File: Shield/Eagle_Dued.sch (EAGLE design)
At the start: 36 parts

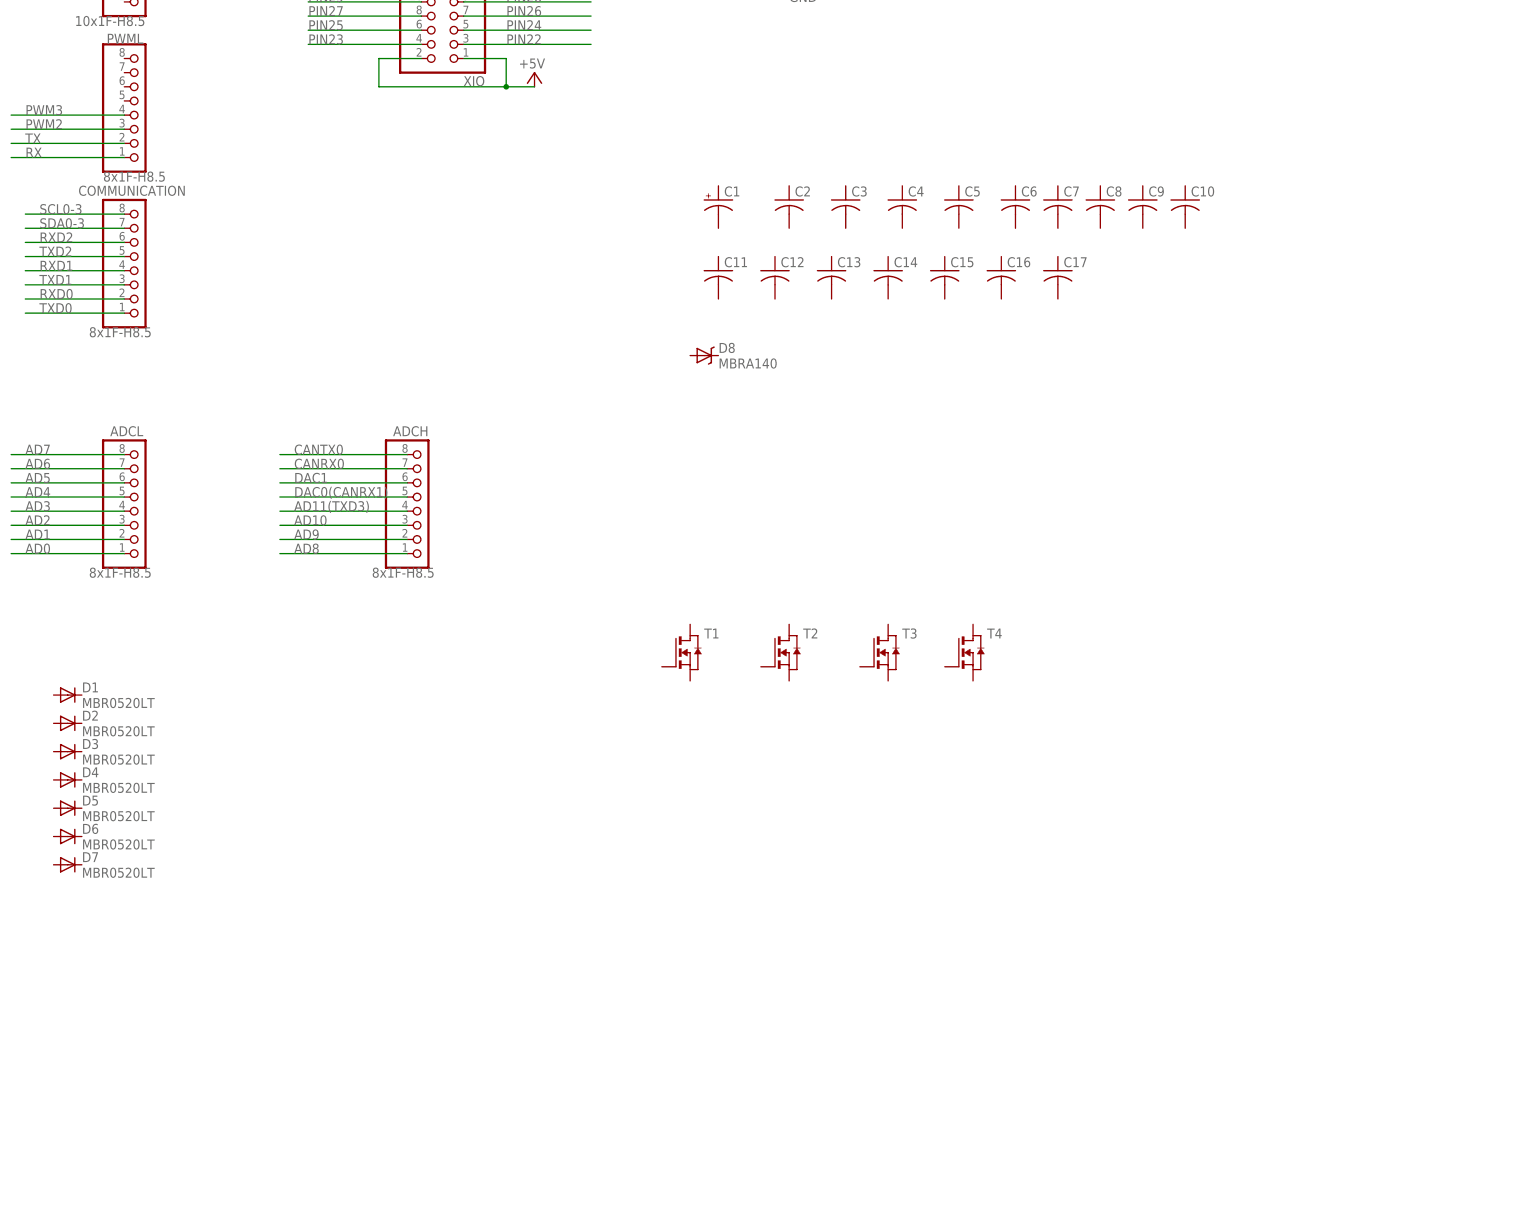
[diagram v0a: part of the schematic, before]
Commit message: More updates to schematic for Shield
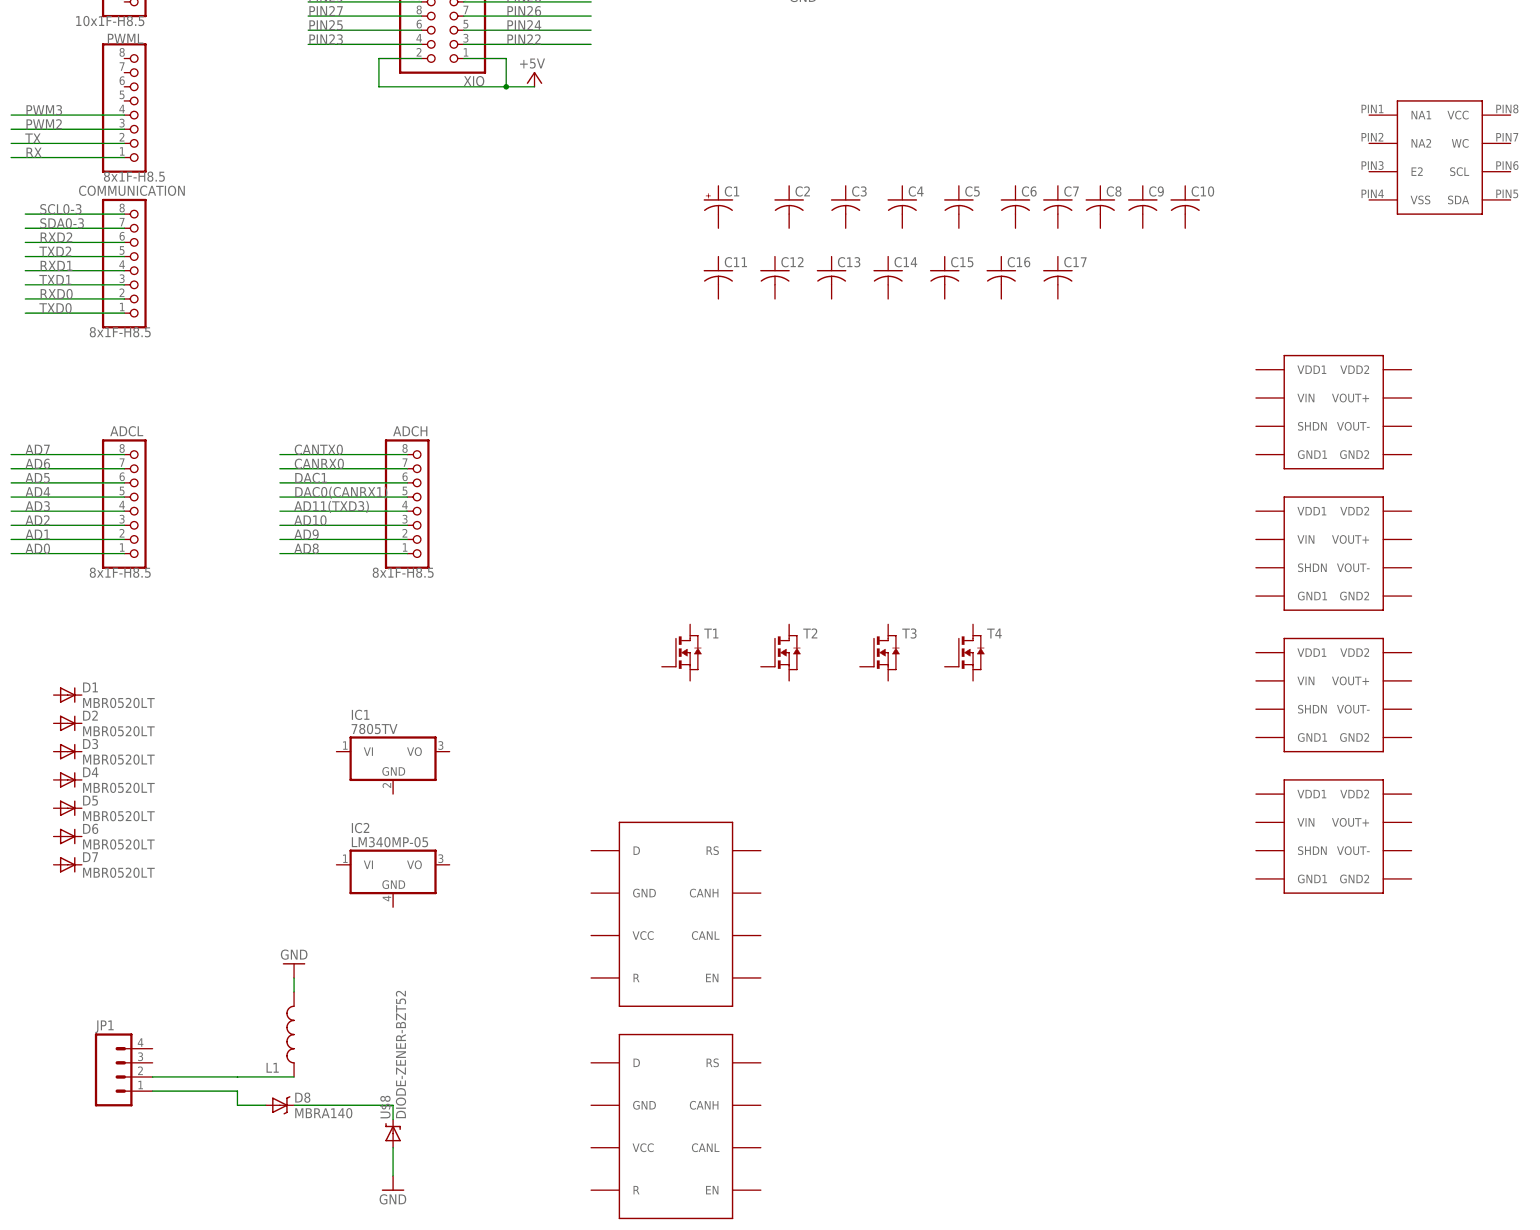
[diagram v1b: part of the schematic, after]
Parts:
- added IC1: 7805TV, linear:7805TV
- added IC2: LM340MP-05, linear:LM340MP-05
- added JP1: (no value), SparkFun-Connectors:M04PTH
- added L1: (no value), SparkFun-Passives:INDUCTOR1206H*
- added U$1, U$2, U$3, U$4: ACPL-C87A-000E, ck_custom:ACPL-C87A-000E
- added U$5: M24M02-DRMN6TP, ck_custom:M24M02-DRMN6TP
- added U$6, U$7: SN65HVD234, ck_custom:SN65HVD234
- added U$8: DIODE-ZENER-BZT52, SparkFun-DiscreteSemi:DIODE-ZENER-BZT52
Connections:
- new net N$1: JP1.2, L1.1
- new net N$2: D8.A, JP1.1
- new net N$3: D8.C, U$8.C
- net GND: now also L1.2, U$8.A
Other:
- moved on the sheet: D8
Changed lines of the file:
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@@
 <part name="C17" library="rcl" deviceset="C-US" device="C0603"/>
 <part name="D8" library="SparkFun-DiscreteSemi" deviceset="MBRA140" device=""/>
+<part name="U$1" library="ck_custom" deviceset="ACPL-C87A-000E" device=""/>
+<part name="U$2" library="ck_custom" deviceset="ACPL-C87A-000E" device=""/>
+<part name="U$3" library="ck_custom" deviceset="ACPL-C87A-000E" device=""/>
+<part name="U$4" library="ck_custom" deviceset="ACPL-C87A-000E" device=""/>
+<part name="U$5" library="ck_custom" deviceset="M24M02-DRMN6TP" device=""/>
+<part name="U$6" library="ck_custom" deviceset="SN65HVD234" device=""/>
+<part name="U$7" library="ck_custom" deviceset="SN65HVD234" device=""/>
+<part name="IC1" library="linear" deviceset="78*" device="TV" technology="05"/>
+<part name="IC2" library="linear" deviceset="LM340?-*" device="MP" technology="05"/>
+<part name="L1" library="SparkFun-Passives" deviceset="INDUCTOR" device="H*" technology="1206"/>
+<part name="JP1" library="SparkFun-Connectors" deviceset="M04" device="PTH"/>
+<part name="GND1" library="supply1" deviceset="GND" device=""/>
+<part name="U$8" library="SparkFun-DiscreteSemi" deviceset="DIODE-ZENER" device="-BZT52"/>
+<part name="GND2" library="supply1" deviceset="GND" device=""/>
 </parts>
 <sheets>
@@
 <instance part="C16" gate="G$1" x="464.82" y="119.38"/>
 <instance part="C17" gate="G$1" x="474.98" y="119.38"/>
-<instance part="D8" gate="G$1" x="411.48" y="104.14"/>
+<instance part="D8" gate="G$1" x="335.28" y="-30.48"/>
+<instance part="U$1" gate="G$1" x="515.62" y="83.82"/>
+<instance part="U$2" gate="G$1" x="515.62" y="58.42"/>
+<instance part="U$3" gate="G$1" x="515.62" y="33.02"/>
+<instance part="U$4" gate="G$1" x="515.62" y="7.62"/>
+<instance part="U$5" gate="G$1" x="535.94" y="129.54"/>
+<instance part="U$6" gate="G$1" x="396.24" y="-12.7"/>
+<instance part="U$7" gate="G$1" x="396.24" y="-50.8"/>
+<instance part="IC1" gate="A1" x="355.6" y="33.02"/>
+<instance part="IC2" gate="A" x="355.6" y="12.7"/>
+<instance part="L1" gate="G$1" x="337.82" y="-17.78" rot="R180"/>
+<instance part="JP1" gate="G$1" x="307.34" y="-25.4"/>
+<instance part="GND1" gate="1" x="337.82" y="-5.08" rot="R180"/>
+<instance part="U$8" gate="G$1" x="355.6" y="-35.56" rot="R90"/>
+<instance part="GND2" gate="1" x="355.6" y="-45.72"/>
 </instances>
 <busses>
@@
 <pinref part="GND6" gate="1" pin="GND"/>
 </segment>
+<segment>
+<pinref part="L1" gate="G$1" pin="2"/>
+<pinref part="GND1" gate="1" pin="GND"/>
+<wire x1="337.82" y1="-10.16" x2="337.82" y2="-7.62" width="0.1524" layer="91"/>
+</segment>
+<segment>
+<pinref part="U$8" gate="G$1" pin="A"/>
+<pinref part="GND2" gate="1" pin="GND"/>
+<wire x1="355.6" y1="-38.1" x2="355.6" y2="-43.18" width="0.1524" layer="91"/>
+</segment>
 </net>
 <net name="VIN" class="0">
@@
 </segment>
 </net>
+<net name="N$1" class="0">
+<segment>
+<pinref part="JP1" gate="G$1" pin="2"/>
+<wire x1="312.42" y1="-25.4" x2="327.66" y2="-25.4" width="0.1524" layer="91"/>
+<pinref part="L1" gate="G$1" pin="1"/>
+<wire x1="327.66" y1="-25.4" x2="337.82" y2="-25.4" width="0.1524" layer="91"/>
+</segment>
+</net>
+<net name="N$2" class="0">
+<segment>
+<pinref part="JP1" gate="G$1" pin="1"/>
+<wire x1="312.42" y1="-27.94" x2="327.66" y2="-27.94" width="0.1524" layer="91"/>
+<wire x1="327.66" y1="-27.94" x2="327.66" y2="-30.48" width="0.1524" layer="91"/>
+<pinref part="D8" gate="G$1" pin="A"/>
+<wire x1="327.66" y1="-30.48" x2="332.74" y2="-30.48" width="0.1524" layer="91"/>
+</segment>
+</net>
+<net name="N$3" class="0">
+<segment>
+<pinref part="D8" gate="G$1" pin="C"/>
+<wire x1="337.82" y1="-30.48" x2="355.6" y2="-30.48" width="0.1524" layer="91"/>
+<pinref part="U$8" gate="G$1" pin="C"/>
+<wire x1="355.6" y1="-30.48" x2="355.6" y2="-33.02" width="0.1524" layer="91"/>
+</segment>
+</net>
